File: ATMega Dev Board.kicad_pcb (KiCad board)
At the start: 4 copper layers, 84 x 38.1 mm, 40 parts, among them J1 Conn_01x09, J2 Conn_01x04, J3 Conn_01x09, J4 SPI header, J5 USB-C_31-M-12, Q1 S8050, SW1 SW_SPST, SW2 SW_SPST, U1 ATmega32A-A, U2 CH340C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

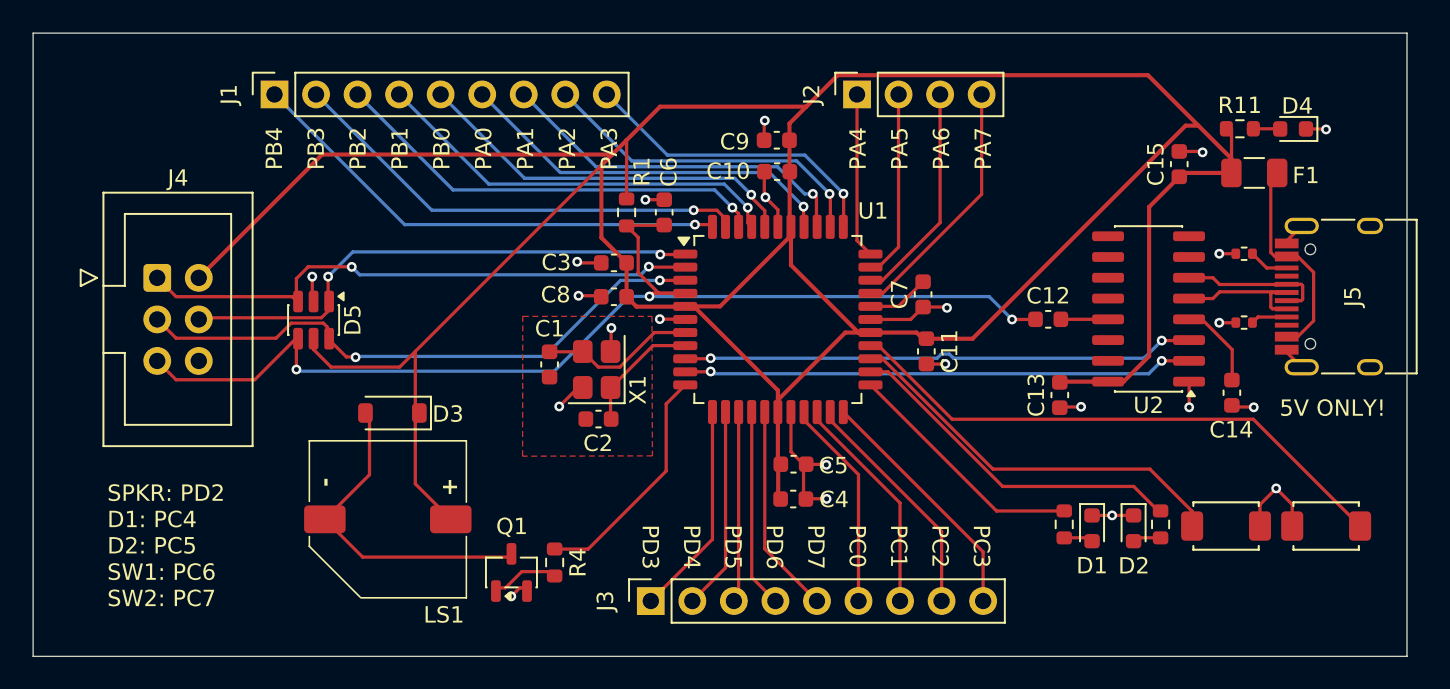
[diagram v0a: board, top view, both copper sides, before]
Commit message: Improved VCC routing
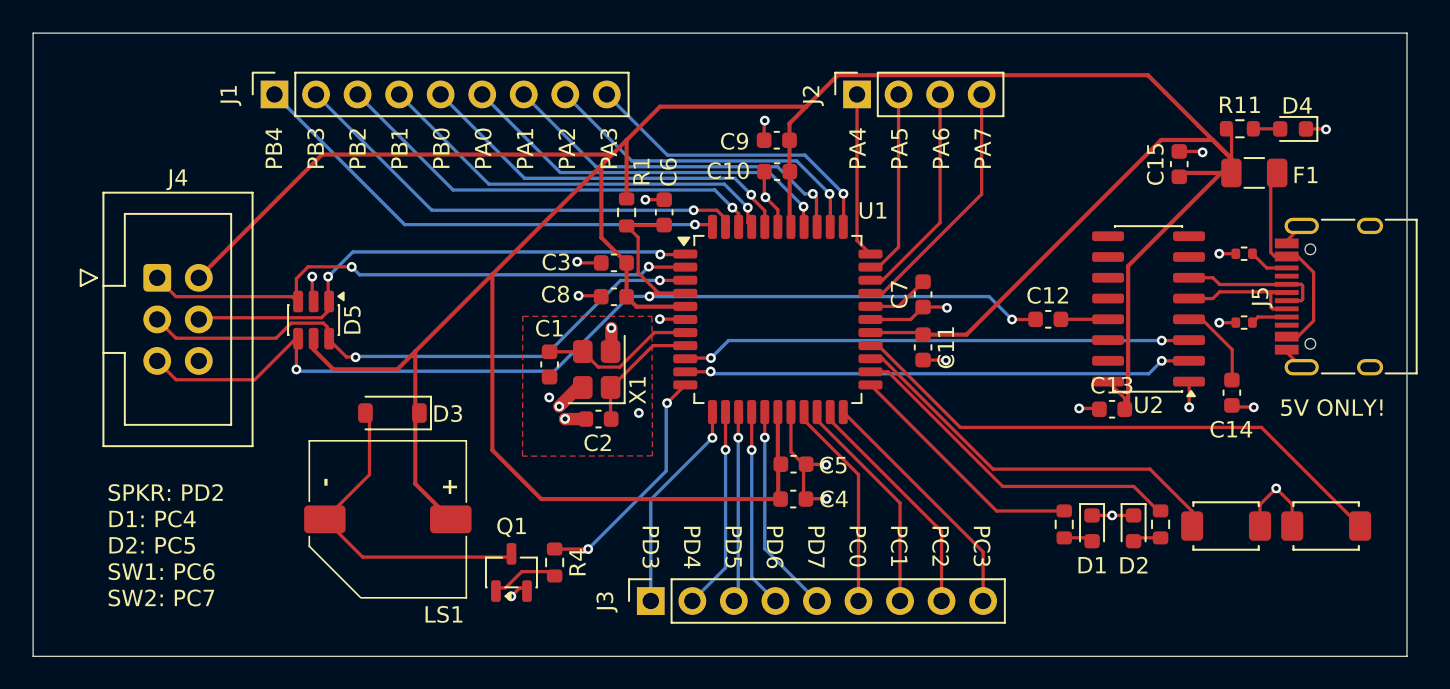
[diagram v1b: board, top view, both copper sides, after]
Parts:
- J5: footprint Connector_USB:USB_C_Receptacle_HRO_TYPE-C-31-M-12 -> FTBLib:USB_C_Receptacle_HRO_TYPE-C-31-M-12
- moved C13 3.31 mm to (144.0, 95.6), turned to 0 degrees
- moved C11 0.32 mm to (132.5, 91.9)
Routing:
- net GND: track 51.0 -> 52.6 mm, vias 23 -> 26
- net VCC: track 220.7 -> 219.3 mm
- net /SPKR: vias 0 -> 2
- net /PD7: vias 0 -> 1
- net /PD6: vias 0 -> 1
- net /PD5: vias 0 -> 1
- net /PD4: vias 0 -> 1
- net /PD3: vias 0 -> 1

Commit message: Small footprint changes
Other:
- board text added: "Rev A - Feb 2026 github.com/spassigl/ATMega32A-simple-board.git"
- board text removed: "ATMega32A test board Rev A"
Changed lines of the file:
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@@
 		)
 	)
-	(gr_text "ATMega32A test board\nRev A"
-		(at 96.69 109.02 -0)
+	(gr_text "Rev A - Feb 2026\ngithub.com/spassigl/ATMega32A-simple-board.git"
+		(at 139.68 102.69 0)
 		(layer "B.SilkS")
 		(effects

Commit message: Better traces
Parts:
- removed C6: 0.1u, Capacitor_SMD:C_0603_1608Metric
- R1: value 4k7 -> 10k
- moved R1 4.19 mm to (116.0, 87.4)
- moved C15 0.61 mm to (147.9, 81.2), turned to 180 degrees
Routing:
- net /RST: track 70.5 -> 63.6 mm
- net VCC: track 219.3 -> 212.6 mm
- net /MISO: track 35.0 -> 39.8 mm
- net /MOSI: track 32.8 -> 36.3 mm
- net /SCK: track 36.3 -> 38.6 mm
- net GND: track 52.6 -> 51.3 mm, vias 26 -> 25
- net /PD3: track 13.1 -> 14.3 mm
- net Net-(F1-Pad2): track 13.2 -> 13.8 mm
- net /PA5: vias 0 -> 1
- net /PA6: track 13.6 -> 13.5 mm, vias 0 -> 1
- net /PA7: vias 0 -> 1
- net /PA4: vias 0 -> 1
